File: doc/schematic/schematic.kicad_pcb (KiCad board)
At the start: 2 copper layers, 11 parts, among them J1 Conn_01x03_Pin, J14 Conn_01x02_Pin, J15 FX35, J18 Conn_01x02_Pin, J19 Conn_01x02_Pin, J2 Conn_01x03_Socket, J3 Conn_01x05_Pin, J7 INA, U1 ESP32-S3-DevKitC, U3 INA219(0x41)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

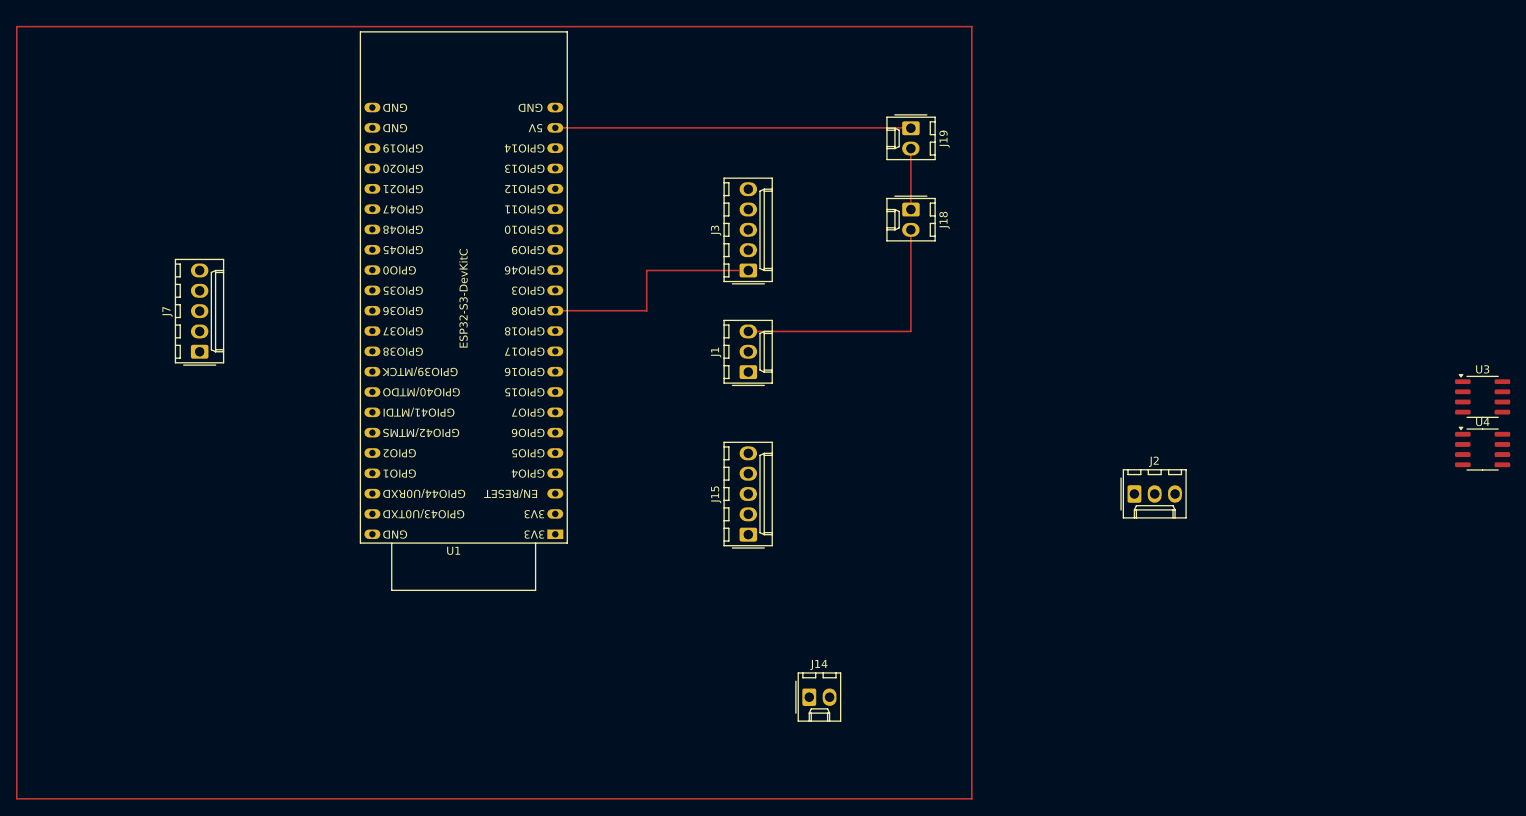
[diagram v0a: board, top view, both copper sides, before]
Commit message: Add 2nd INA219 & modify display.
ToDo: implementation of FZ35
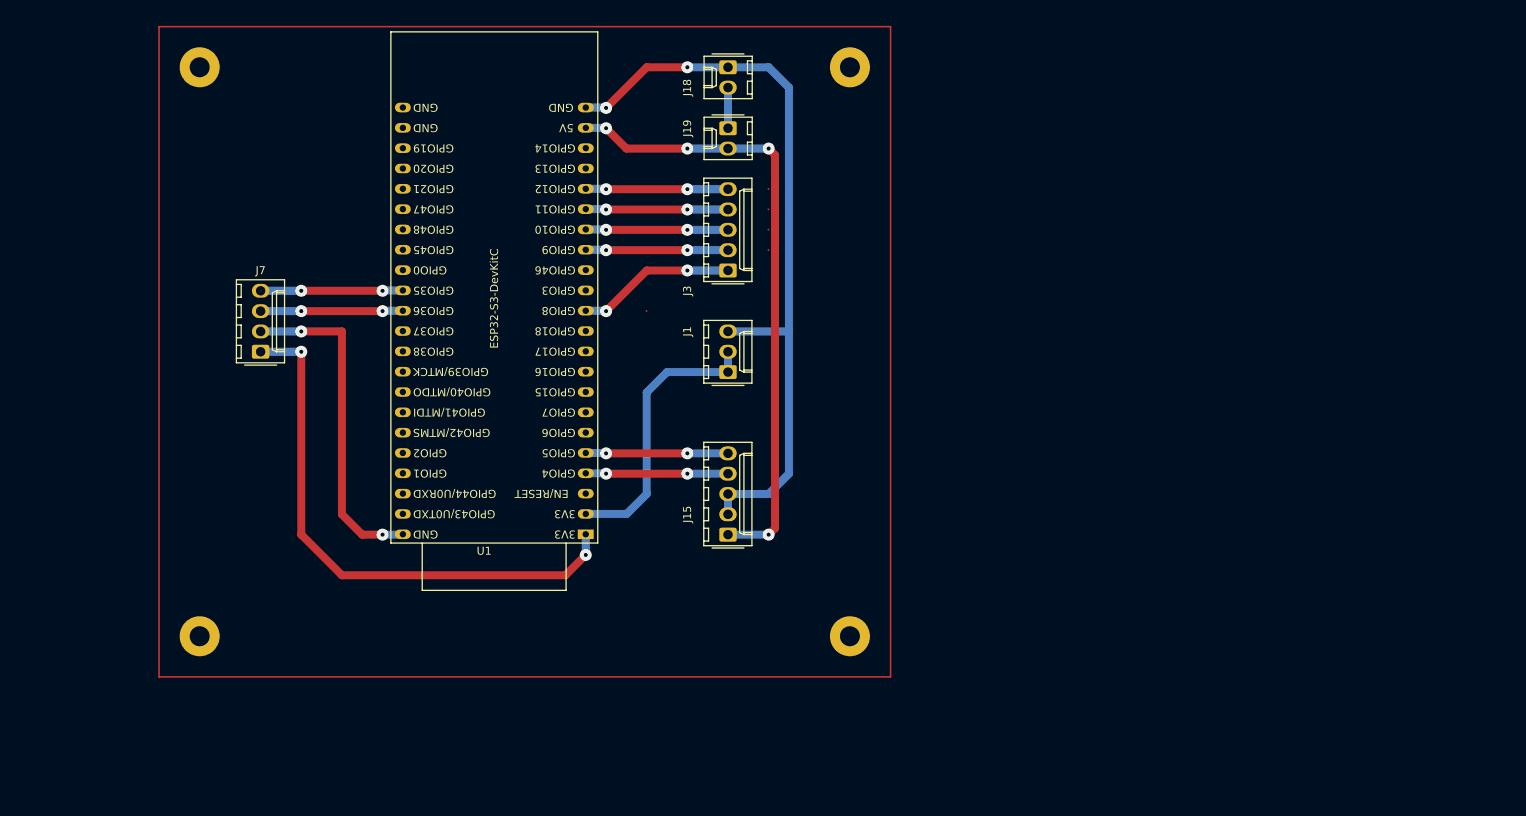
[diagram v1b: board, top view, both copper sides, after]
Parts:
- removed J14: Conn_01x02_Pin, Connector_Molex:Molex_KK-254_AE-6410-02A_1x02_P2.54mm_Vertical
- removed J2: Conn_01x03_Socket, Connector_Molex:Molex_KK-254_AE-6410-03A_1x03_P2.54mm_Vertical
- removed U3: INA219(0x41), Package_SO:SOIC-8_3.9x4.9mm_P1.27mm
- removed U4: INA219(0x40), Package_SO:SOIC-8_3.9x4.9mm_P1.27mm
- added REF**: MountingHole_2.5mm_Pad, MountingHole:MountingHole_2.5mm_Pad, F.Cu at (154.9, 55.9)
- added REF**: MountingHole_2.5mm_Pad, MountingHole:MountingHole_2.5mm_Pad, F.Cu at (154.9, 127.0)
- added REF**: MountingHole_2.5mm_Pad, MountingHole:MountingHole_2.5mm_Pad, F.Cu at (73.7, 55.9)
- added REF**: MountingHole_2.5mm_Pad, MountingHole:MountingHole_2.5mm_Pad, F.Cu at (73.7, 127.0)
- J1: value Conn_01x03_Pin -> TFT_Power
- J15: value FX35 -> fz35
- J18: value Conn_01x02_Pin -> USB
- J19: value Conn_01x02_Pin -> Switch
- J3: value Conn_01x05_Pin -> TFT
- J7: footprint Connector_Molex:Molex_KK-254_AE-6410-05A_1x05_P2.54mm_Vertical -> Connector_Molex:Molex_KK-254_AE-6410-04A_1x04_P2.54mm_Vertical
- moved J18 29.0 mm to (139.7, 55.9)
- moved J19 22.9 mm to (139.7, 63.5)
- moved J7 7.62 mm to (81.3, 91.4)
- moved U1 3.81 mm to (121.9, 114.3)
- moved J1 2.54 mm to (139.7, 94.0)
- moved J15 2.54 mm to (139.7, 114.3)
- moved J3 2.54 mm to (139.7, 81.3)
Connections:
- J18 pad 1: Net-(J18-Pin_1) -> GND
- J18 pad 2: GND -> Net-(J18-Pin_2)
- J19 pad 1: +5V -> Net-(J18-Pin_2)
- J19 pad 2: Net-(J18-Pin_1) -> +5V
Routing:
- net GND: track 33.0 -> 137.4 mm, vias 0 -> 4
- net +3V3: track 0.00 -> 104.3 mm, vias 0 -> 2
- net +5V: track 44.5 -> 77.9 mm, vias 0 -> 4
- net Net-(J7-Pin_3): track 0.00 -> 17.8 mm, vias 0 -> 2
- net Net-(J7-Pin_4): track 0.00 -> 17.8 mm, vias 0 -> 2
- net Net-(J15-Pin_5): track 0.00 -> 17.8 mm, vias 0 -> 2
- net Net-(J15-Pin_4): track 0.00 -> 17.8 mm, vias 0 -> 2
- net Net-(J3-Pin_5): track 0.07 -> 17.9 mm, vias 0 -> 2
- net Net-(J3-Pin_3): track 0.07 -> 17.9 mm, vias 0 -> 2
- net Net-(J3-Pin_4): track 0.07 -> 17.9 mm, vias 0 -> 2
- net Net-(J3-Pin_2): track 0.07 -> 17.9 mm, vias 0 -> 2
- net Net-(J3-Pin_1): track 29.2 -> 20.0 mm, vias 0 -> 2
- net Net-(J18-Pin_1): track 7.62 -> 0.00 mm
- net Net-(J18-Pin_2): track 0.00 -> 5.08 mm

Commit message: full functionality
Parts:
- added J22: Fan, Connector_Molex:Molex_KK-254_AE-6410-02A_1x02_P2.54mm_Vertical, F.Cu at (142.2, 73.7)
- moved J3 9.25 mm to (142.2, 90.2)
- moved J7 9.16 mm to (76.2, 99.1), turned to -90 degrees
- moved REF** 8.98 mm to (72.4, 118.1)
- moved REF** 8.89 mm to (154.9, 118.1)
- moved U1 7.62 mm to (114.3, 114.3)
- moved J1 6.84 mm to (142.2, 100.3)
- moved J15 3.59 mm to (142.2, 116.8)
- moved J18 2.54 mm to (142.2, 55.9)
- moved J19 2.54 mm to (142.2, 63.5)
- moved REF** 1.80 mm to (72.4, 54.6)
- moved REF** 1.27 mm to (154.9, 54.6)
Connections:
- U1 pad 23: GND -> unconnected-(U1-GND-Pad23)
- U1 pad 24: GND -> unconnected-(U1-GND-Pad24)
- U1 pad 32: Net-(J7-Pin_4) -> unconnected-(U1-GPIO35-Pad32)
- U1 pad 33: Net-(J7-Pin_3) -> unconnected-(U1-GPIO36-Pad33)
- U1 pad 40: unconnected-(U1-GPIO2/ADC1_CH1-Pad40) -> Net-(J7-Pin_3)
- U1 pad 41: unconnected-(U1-GPIO1/ADC1_CH0-Pad41) -> Net-(J7-Pin_4)
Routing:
- net GND: track 137.4 -> 161.1 mm, vias 4 -> 0
- net +5V: track 77.9 -> 95.1 mm, vias 4 -> 2
- net Net-(J3-Pin_5): track 17.9 -> 31.7 mm
- net Net-(J3-Pin_3): track 17.9 -> 31.7 mm
- net Net-(J3-Pin_4): track 17.9 -> 31.7 mm
- net Net-(J3-Pin_2): track 17.9 -> 31.7 mm
- net Net-(J15-Pin_5): track 17.8 -> 29.0 mm
- net Net-(J15-Pin_4): track 17.8 -> 29.0 mm
- net Net-(J3-Pin_1): track 20.0 -> 29.6 mm
- net +3V3: track 104.3 -> 107.0 mm
- net Net-(J7-Pin_3): track 17.8 -> 15.2 mm
- net Net-(J7-Pin_4): track 17.8 -> 15.2 mm
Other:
- board outline added: 90.2 x 71.1 mm

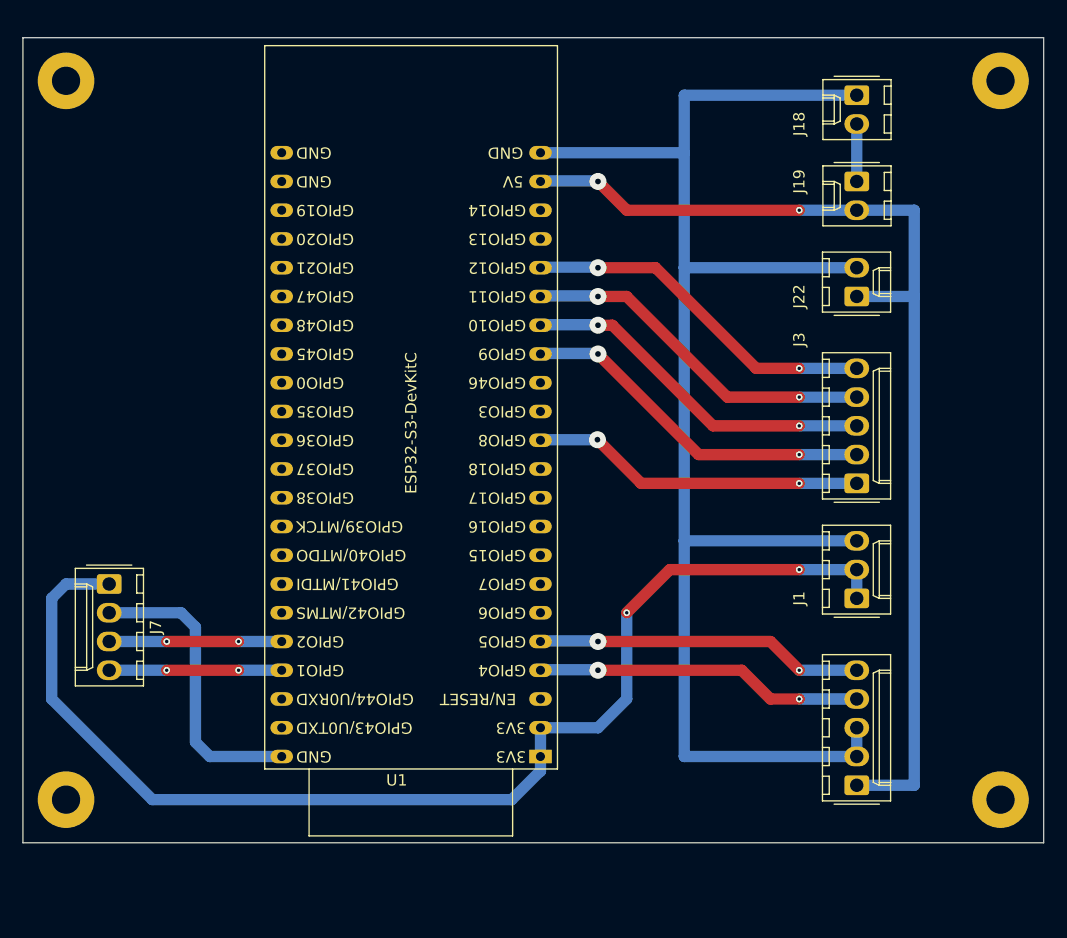
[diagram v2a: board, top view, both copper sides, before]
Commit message: code optimization
1.) centralization of data in a global class
2.) make Display as a global class
3.) code optimization
4.) prepare for a setup dialog

this version not able for production
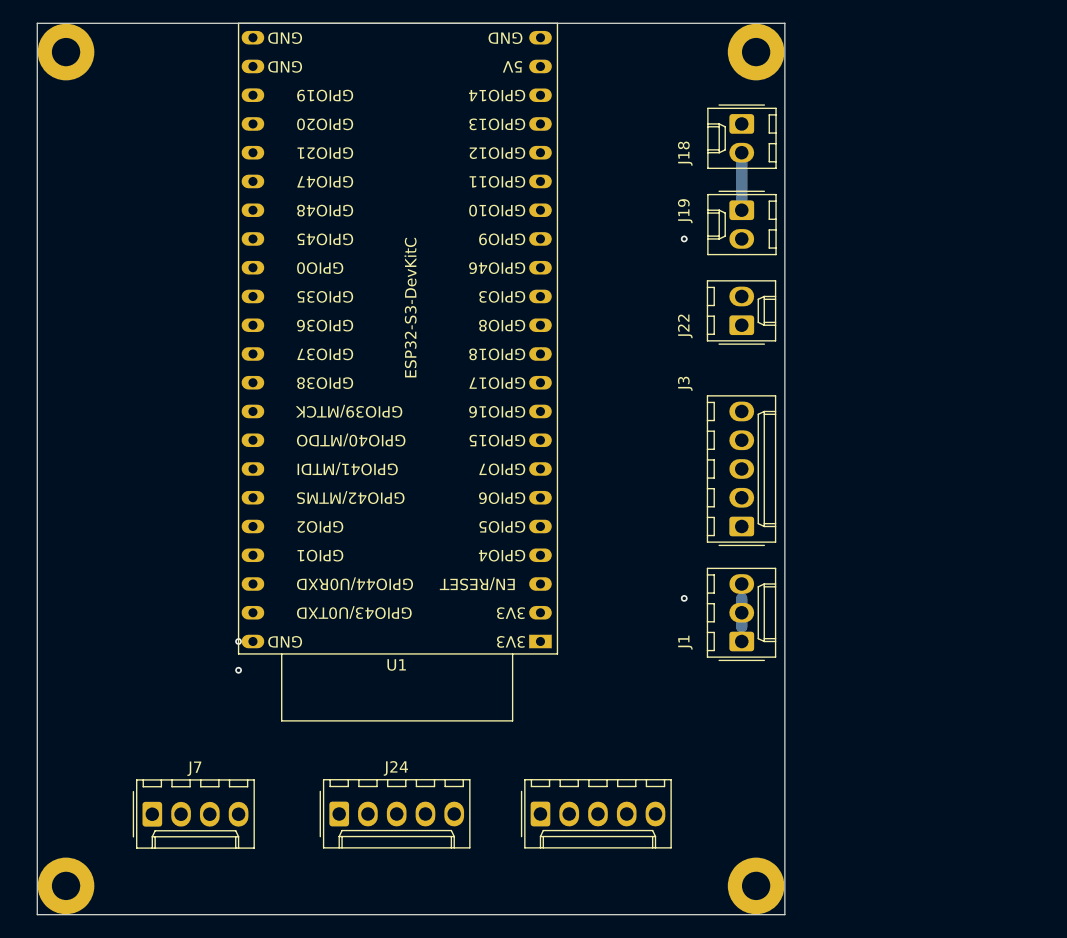
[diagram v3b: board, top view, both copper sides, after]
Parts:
- added J24: KY-040, Connector_Molex:Molex_KK-254_AE-6410-05A_1x05_P2.54mm_Vertical, F.Cu at (96.5, 119.4)
- U1: footprint PCM_Espressif:ESP32-S3-DevKitC -> Library:ESP32-S3-DevKitC
- moved J15 28.1 mm to (114.3, 119.4), turned to 0 degrees
- moved REF** 22.9 mm to (133.3, 125.7)
- moved REF** 21.7 mm to (133.3, 52.1)
- moved J7 20.7 mm to (80.0, 119.4), turned to 0 degrees
- moved J1 10.9 mm to (132.1, 104.1)
- moved J3 10.9 mm to (132.1, 94.0)
- moved J19 10.5 mm to (132.1, 66.0)
- moved J22 10.5 mm to (132.1, 76.2)
- moved J18 10.5 mm to (132.1, 58.4)
- moved U1 10.2 mm to (114.3, 104.1)
- moved REF** 7.62 mm to (72.4, 125.7)
- moved REF** 2.54 mm to (72.4, 52.1)
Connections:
- U1 pad 6: unconnected-(U1-GPIO6/ADC1_CH5-Pad6) -> Net-(J24-Pin_1)
- U1 pad 7: unconnected-(U1-GPIO7/ADC1_CH6-Pad7) -> Net-(J24-Pin_2)
- U1 pad 8: unconnected-(U1-GPIO15/ADC2_CH4/32K_P-Pad8) -> Net-(J24-Pin_3)
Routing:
- net GND: track 161.1 -> 0.00 mm, vias 0 -> 1
- net +3V3: track 107.0 -> 2.61 mm, vias 2 -> 1
- net +5V: track 95.1 -> 0.00 mm, vias 2 -> 1
- net Net-(J3-Pin_3): track 31.7 -> 0.00 mm, vias 2 -> 0
- net Net-(J3-Pin_2): track 31.7 -> 0.00 mm, vias 2 -> 0
- net Net-(J3-Pin_5): track 31.7 -> 0.07 mm, vias 2 -> 0
- net Net-(J3-Pin_4): track 31.7 -> 0.07 mm, vias 2 -> 0
- net Net-(J3-Pin_1): track 29.6 -> 0.07 mm, vias 2 -> 0
- net Net-(J15-Pin_5): track 29.0 -> 0.00 mm, vias 2 -> 0
- net Net-(J15-Pin_4): track 29.0 -> 0.00 mm, vias 2 -> 0
- net Net-(J7-Pin_4): track 15.2 -> 0.00 mm, vias 2 -> 1
- net Net-(J7-Pin_3): track 15.2 -> 0.00 mm, vias 2 -> 0
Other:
- board size 90.2 x 71.1 mm -> 66 x 78.7 mm

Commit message: update schematic
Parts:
- moved U1 7.62 mm to (106.7, 104.1)
- moved J1 5.08 mm to (127.0, 104.1)
- moved J18 5.08 mm to (127.0, 58.4)
- moved J19 5.08 mm to (127.0, 66.0)
- moved J22 5.08 mm to (127.0, 76.2)
- moved J3 5.08 mm to (127.0, 94.0)
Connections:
- U1 pad 40: Net-(J7-Pin_3) -> Net-(J7-Pin_4)
- U1 pad 41: Net-(J7-Pin_4) -> Net-(J7-Pin_3)
- U1 pad 6: Net-(J24-Pin_1) -> Net-(J24-Pin_3)
- U1 pad 8: Net-(J24-Pin_3) -> Net-(J24-Pin_1)
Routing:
- net GND: track 0.00 -> 152.5 mm, vias 1 -> 2
- net +5V: track 0.00 -> 121.7 mm, vias 1 -> 2
- net +3V3: track 2.61 -> 71.2 mm, vias 1 -> 0
- net Net-(J3-Pin_3): track 0.00 -> 39.2 mm, vias 0 -> 2
- net Net-(J3-Pin_5): track 0.07 -> 39.1 mm, vias 0 -> 2
- net Net-(J3-Pin_4): track 0.07 -> 39.1 mm, vias 0 -> 2
- net Net-(J24-Pin_1): track 0.00 -> 38.7 mm
- net Net-(J3-Pin_2): track 0.00 -> 38.7 mm, vias 0 -> 2
- net Net-(J15-Pin_5): track 0.00 -> 35.7 mm, vias 0 -> 2
- net Net-(J24-Pin_2): track 0.00 -> 35.1 mm
- net Net-(J3-Pin_1): track 0.07 -> 34.0 mm, vias 0 -> 2
- net Net-(J24-Pin_3): track 0.07 -> 31.5 mm
- net Net-(J7-Pin_4): track 0.00 -> 31.0 mm, vias 1 -> 0
- net Net-(J15-Pin_4): track 0.00 -> 30.7 mm, vias 0 -> 2
- net Net-(J7-Pin_3): track 0.00 -> 25.9 mm

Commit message: Bug Fix for V1.0.0-pre_alpha
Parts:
- added C1: 0,1µ, Capacitor_THT:C_Axial_L3.8mm_D2.6mm_P7.50mm_Horizontal, F.Cu at (150.0, 109.2)
- moved J7 1.27 mm to (78.7, 119.4)
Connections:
- J7 pad 1: +3V3 -> Net-(J7-Pin_1)
- J7 pad 2: GND -> Net-(J7-Pin_2)
- J7 pad 3: Net-(J7-Pin_3) -> GND
- J7 pad 4: Net-(J7-Pin_4) -> +3V3
- U1 pad 40: Net-(J7-Pin_4) -> Net-(J7-Pin_1)
- U1 pad 41: Net-(J7-Pin_3) -> Net-(J7-Pin_2)
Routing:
- net Net-(J7-Pin_1): track 0.00 -> 31.5 mm, vias 0 -> 2
- net Net-(J7-Pin_4): track 31.0 -> 0.00 mm
- net Net-(J7-Pin_2): track 0.00 -> 26.5 mm, vias 0 -> 2
- net Net-(J7-Pin_3): track 25.9 -> 0.00 mm
- net GND: track 152.5 -> 141.8 mm, vias 2 -> 3
- net +3V3: track 71.2 -> 77.3 mm, vias 0 -> 2
